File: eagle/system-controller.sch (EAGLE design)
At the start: 232 parts, among them CN1 22u, IC2 TS4100, J1 1, Q0 MOSFET-P-N-PAIR, Q1 MOSFET-P-N-PAIR, Q10 DNP/NTR4101P, Q12 DNP/NTR4101P, Q13 DON3035L, Q2 MOSFET-P-N-PAIR, Q3 MOSFET-P-N-PAIR, Q4 MOSFET-P-N-PAIR, Q5 MOSFET-P-N-PAIR, Q6 MOSFET-P-N-PAIR, Q7 MOSFET-P-N-PAIR, SW0 TPS25944LRVCRWQFN-20-3X4, SW1 TPS25944LRVCRWQFN-20-3X4, SW2 TPS25944LRVCRWQFN-20-3X4, SW3 TPS25944LRVCRWQFN-20-3X4, SW4 TPS25944LRVCRWQFN-20-3X4, SW5 TPS25944LRVCRWQFN-20-3X4, SW6 TPS25944LRVCRWQFN-20-3X4, SW7 TPS25944LRVCRWQFN-20-3X4, U1 MEGA128-A, X1 8 MHz CRYSTAL-ABRACON-ABM3-SMD

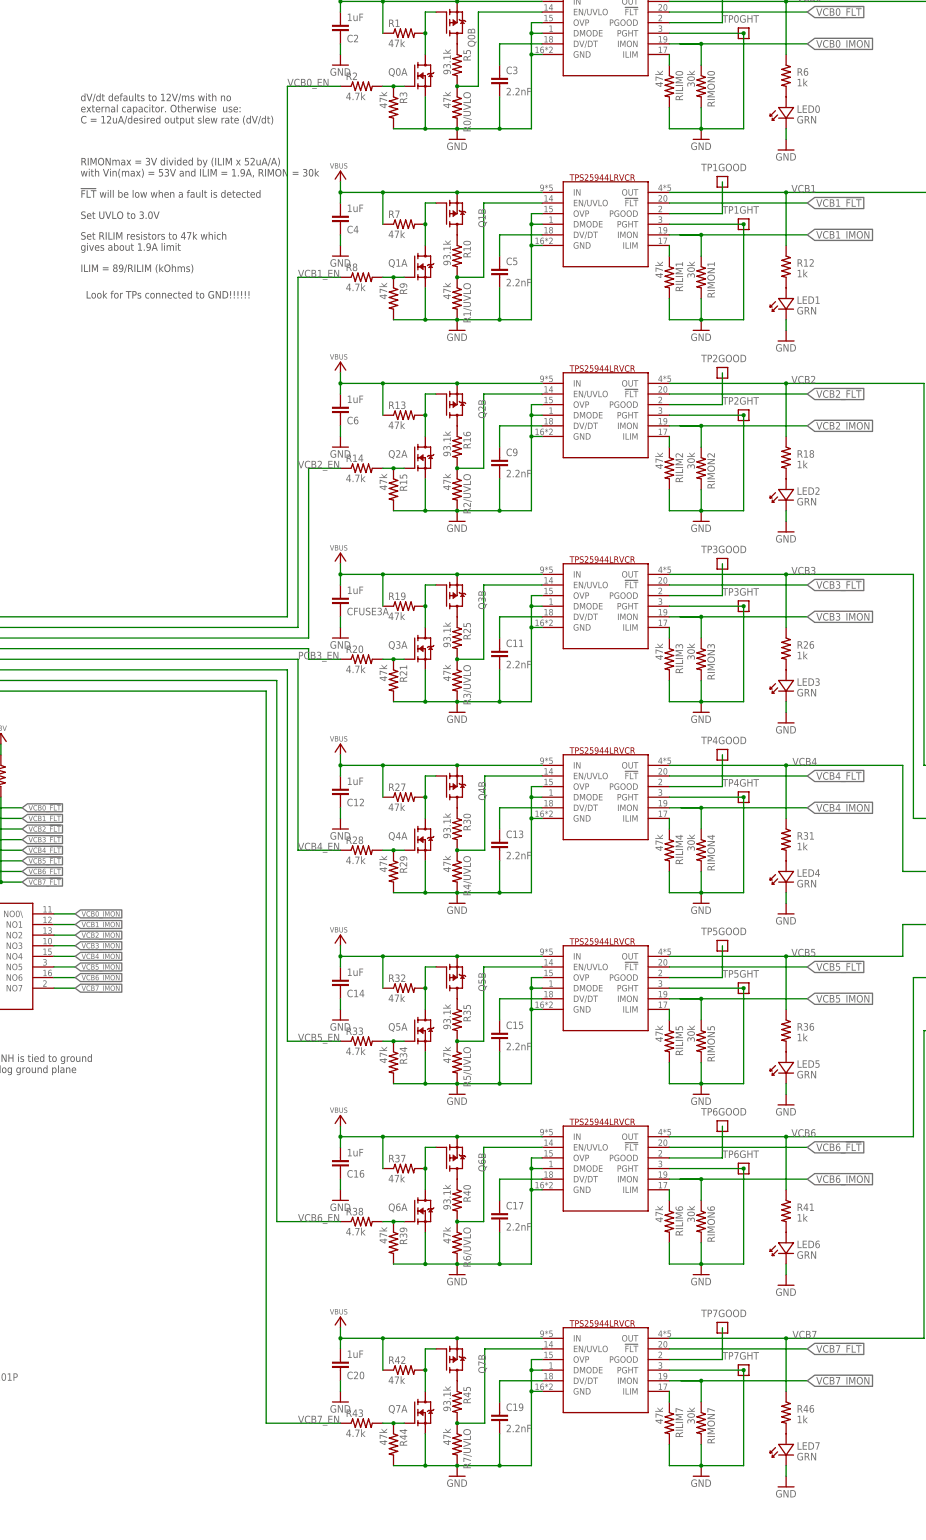
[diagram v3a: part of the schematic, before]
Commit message: Better layout for bypass caps ner AVR. Some cleanup on routing. Changed power domain indicators to DNP.
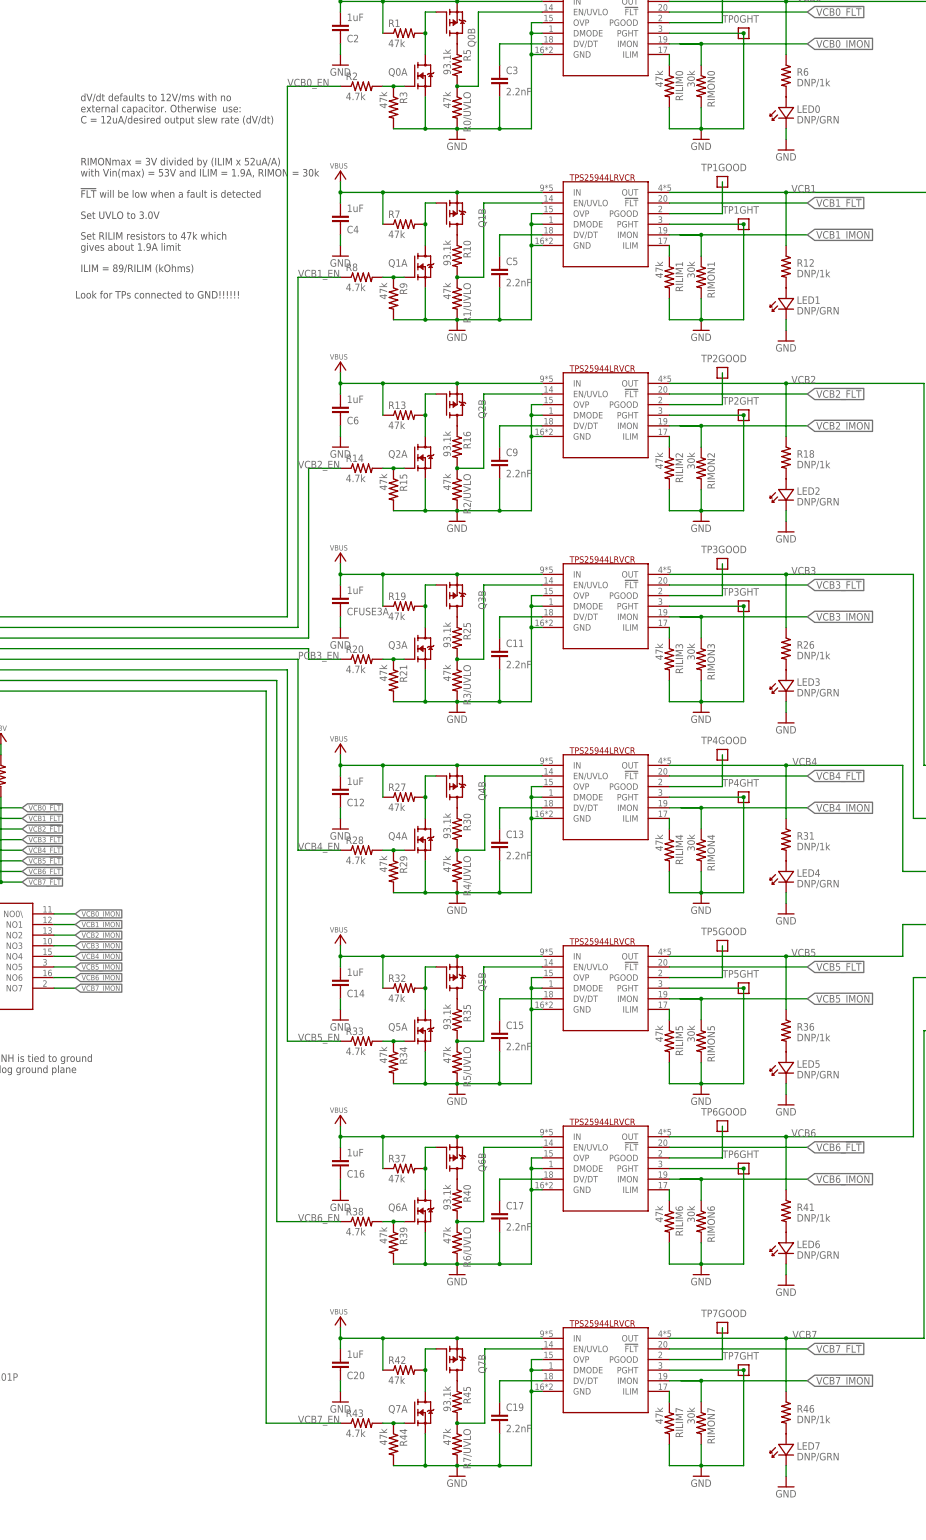
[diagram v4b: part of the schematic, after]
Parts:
- LED0, LED1, LED2, LED3, LED4, LED5, LED6, LED7: value GRN -> DNP/GRN
- R12, R18, R26, R31, R36, R41, R46, R6: value 1k -> DNP/1k
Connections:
- net N$36 renamed AREF
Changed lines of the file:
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@@
 <part name="3V-2" library="supply-3v" deviceset="3V" device=""/>
 <part name="3V-6" library="supply-3v" deviceset="3V" device=""/>
-<part name="LED0" library="psas_c3_team05" deviceset="LED" device="-0603" value="GRN">
+<part name="LED0" library="psas_c3_team05" deviceset="LED" device="-0603" value="DNP/GRN">
 <attribute name="DIST" value="digikey"/>
 <attribute name="DPN" value="732-4971-1-ND"/>
@@
 <attribute name="MPN" value="150060GS75000"/>
 </part>
-<part name="R6" library="rcl_custom" deviceset="R-US_" device="0603-B-NOSILK" value="1k">
+<part name="R6" library="rcl_custom" deviceset="R-US_" device="0603-B-NOSILK" value="DNP/1k">
 <attribute name="DIST" value="digikey"/>
 <attribute name="DPN" value="1276-3484-1-ND"/>
@@
 <attribute name="MPN" value="RC1608F472CS"/>
 </part>
-<part name="R12" library="rcl_custom" deviceset="R-US_" device="0603-B-NOSILK" value="1k">
+<part name="R12" library="rcl_custom" deviceset="R-US_" device="0603-B-NOSILK" value="DNP/1k">
 <attribute name="DIST" value="digikey"/>
 <attribute name="DPN" value="1276-3484-1-ND"/>
@@
 <attribute name="MPN" value="RC1608F102CS"/>
 </part>
-<part name="R18" library="rcl_custom" deviceset="R-US_" device="0603-B-NOSILK" value="1k">
+<part name="R18" library="rcl_custom" deviceset="R-US_" device="0603-B-NOSILK" value="DNP/1k">
 <attribute name="DIST" value="digikey"/>
 <attribute name="DPN" value="1276-3484-1-ND"/>
@@
 <attribute name="MPN" value="RC1608F102CS"/>
 </part>
-<part name="R26" library="rcl_custom" deviceset="R-US_" device="0603-B-NOSILK" value="1k">
+<part name="R26" library="rcl_custom" deviceset="R-US_" device="0603-B-NOSILK" value="DNP/1k">
 <attribute name="DIST" value="digikey"/>
 <attribute name="DPN" value="1276-3484-1-ND"/>
@@
 <attribute name="MPN" value="RC1608F102CS"/>
 </part>
-<part name="R31" library="rcl_custom" deviceset="R-US_" device="0603-B-NOSILK" value="1k">
+<part name="R31" library="rcl_custom" deviceset="R-US_" device="0603-B-NOSILK" value="DNP/1k">
 <attribute name="DIST" value="digikey"/>
 <attribute name="DPN" value="1276-3484-1-ND"/>
@@
 <attribute name="MPN" value="RC1608F102CS"/>
 </part>
-<part name="R36" library="rcl_custom" deviceset="R-US_" device="0603-B-NOSILK" value="1k">
+<part name="R36" library="rcl_custom" deviceset="R-US_" device="0603-B-NOSILK" value="DNP/1k">
 <attribute name="DIST" value="digikey"/>
 <attribute name="DPN" value="1276-3484-1-ND"/>
@@
 <attribute name="MPN" value="RC1608F102CS"/>
 </part>
-<part name="R41" library="rcl_custom" deviceset="R-US_" device="0603-B-NOSILK" value="1k">
+<part name="R41" library="rcl_custom" deviceset="R-US_" device="0603-B-NOSILK" value="DNP/1k">
 <attribute name="DIST" value="digikey"/>
 <attribute name="DPN" value="1276-3484-1-ND"/>
@@
 <attribute name="MPN" value="RC1608F102CS"/>
 </part>
-<part name="R46" library="rcl_custom" deviceset="R-US_" device="0603-B-NOSILK" value="1k">
+<part name="R46" library="rcl_custom" deviceset="R-US_" device="0603-B-NOSILK" value="DNP/1k">
 <attribute name="DIST" value="digikey"/>
 <attribute name="DPN" value="1276-3484-1-ND"/>
@@
 <attribute name="MPN" value="RC1608F102CS"/>
 </part>
-<part name="LED1" library="psas_c3_team05" deviceset="LED" device="-0603" value="GRN">
+<part name="LED1" library="psas_c3_team05" deviceset="LED" device="-0603" value="DNP/GRN">
 <attribute name="DIST" value="digikey"/>
 <attribute name="DPN" value="732-4971-1-ND"/>
@@
 <attribute name="MPN" value="150060GS75000"/>
 </part>
-<part name="LED2" library="psas_c3_team05" deviceset="LED" device="-0603" value="GRN">
+<part name="LED2" library="psas_c3_team05" deviceset="LED" device="-0603" value="DNP/GRN">
 <attribute name="DIST" value="digikey"/>
 <attribute name="DPN" value="732-4971-1-ND"/>
@@
 <attribute name="MPN" value="150060GS75000"/>
 </part>
-<part name="LED3" library="psas_c3_team05" deviceset="LED" device="-0603" value="GRN">
+<part name="LED3" library="psas_c3_team05" deviceset="LED" device="-0603" value="DNP/GRN">
 <attribute name="DIST" value="digikey"/>
 <attribute name="DPN" value="732-4971-1-ND"/>
@@
 <attribute name="MPN" value="150060GS75000"/>
 </part>
-<part name="LED4" library="psas_c3_team05" deviceset="LED" device="-0603" value="GRN">
+<part name="LED4" library="psas_c3_team05" deviceset="LED" device="-0603" value="DNP/GRN">
 <attribute name="DIST" value="digikey"/>
 <attribute name="DPN" value="732-4971-1-ND"/>
@@
 <attribute name="MPN" value="150060GS75000"/>
 </part>
-<part name="LED5" library="psas_c3_team05" deviceset="LED" device="-0603" value="GRN">
+<part name="LED5" library="psas_c3_team05" deviceset="LED" device="-0603" value="DNP/GRN">
 <attribute name="DIST" value="digikey"/>
 <attribute name="DPN" value="732-4971-1-ND"/>
@@
 <attribute name="MPN" value="150060GS75000"/>
 </part>
-<part name="LED6" library="psas_c3_team05" deviceset="LED" device="-0603" value="GRN">
+<part name="LED6" library="psas_c3_team05" deviceset="LED" device="-0603" value="DNP/GRN">
 <attribute name="DIST" value="digikey"/>
 <attribute name="DPN" value="732-4971-1-ND"/>
@@
 <attribute name="MPN" value="150060GS75000"/>
 </part>
-<part name="LED7" library="psas_c3_team05" deviceset="LED" device="-0603" value="GRN">
+<part name="LED7" library="psas_c3_team05" deviceset="LED" device="-0603" value="DNP/GRN">
 <attribute name="DIST" value="digikey"/>
 <attribute name="DPN" value="732-4971-1-ND"/>
@@
 When two pins are high the voltage at TP43 is 1.5V
 When all three pins are high the voltage at TP43 is 0.75V</text>
-<text x="309.88" y="345.44" size="1.778" layer="97">Look for TPs connected to GND!!!!!!</text>
+<text x="307.34" y="345.44" size="1.778" layer="97">Look for TPs connected to GND!!!!!!</text>
 </plain>
 <instances>
@@
 </segment>
 </net>
-<net name="N$36" class="0">
+<net name="AREF" class="0">
 <segment>
 <pinref part="U1" gate="G$1" pin="AREF"/>

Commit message: Added names to missing parts and updated the BOM and Parts Selection doc accordingly
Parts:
- removed U$1, U$2, U$3, U$4: ACPL-M61L, psas_c3_team05:ACPL-M61L
- removed U$8: AAT3215, psas_c3_team05:AAT3215
- added U2: LP5907MFX-3.0, system-controller:LP5907MFX-3.0
- added U3, U4, U5, U6: ACPL-M61L, system-controller:ACPL-M61L
- R17: DIST (none) -> digikey; DPN (none) -> A103093CT-ND; MFN (none) -> TE; MPN (none) -> 4-1676481-5
- renumbered CFUSE3A to C21, CLDO1 to C22, CLDO2 to C23, CLDO3 to C29, CN1 to C24, IC2 to U15, RLDO1 to R60, RN1 to R66, RN2 to R65, RN3 to R64, RN4 to R17, RNR to R62, SW0 to U7, SW1 to U8, SW2 to U9, SW3 to U10, SW4 to U11, SW5 to U12, SW6 to U13, SW7 to U14
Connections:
- net 3V: now also U2.VOUT, U4.VDD, U6.VDD; no longer U$2.VDD, U$4.VDD, U$8.VOUT
- net GND: now also U2.GND, U3.GND2, U4.GND2, U5.GND2, U6.GND2; no longer U$1.GND2, U$2.GND2, U$3.GND2, U$4.GND2, U$8.GND
- net N$16: now also U5.VOUT; no longer U$3.VOUT
- net N$18: now also U6.VOUT; no longer U$4.VOUT
- net N$22: now also U2.EN; no longer U$8.EN
- net N$23: now also U2.BYP; no longer U$8.BYP
- net N$24: now also U4.VOUT; no longer U$2.VOUT
- net N$4: now also U5.VIN; no longer U$3.VIN
- net N$5: now also U3.VOUT; no longer U$1.VOUT
- net N$54: now also U6.VIN; no longer U$4.VIN
- net N$58: now also U3.VIN; no longer U$1.VIN
- net N$8: now also U4.VIN; no longer U$2.VIN
- net TXD0: now also U5.GND1; no longer U$3.GND1
- net TXD1: now also U3.GND1; no longer U$1.GND1
- net UART_FC_TX: now also U4.GND1; no longer U$2.GND1
- net UART_FC_VCC: now also U3.VDD; no longer U$1.VDD
- net UART_LGR_TX: now also U6.GND1; no longer U$4.GND1
- net UART_LGR_VCC: now also U5.VDD; no longer U$3.VDD
- net V+: now also U2.VIN; no longer U$8.VIN

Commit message: More board cleanup!
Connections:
- net GND: now also CF3.19, CF3.29, CF3.39, CF3.9; no longer CF3.15, CF3.25, CF3.35, CF3.5
- net VCB1: now also CF3.5; no longer CF3.9
- net VCB3: now also CF3.15; no longer CF3.19
- net VCB5: now also CF3.25; no longer CF3.29
- net VCB7: now also CF3.35; no longer CF3.39

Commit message: Lots of board cleanup. Improved packages for ATMEGA, analog switch, and TPS. Re-did power polygons to tighten up the layout. Straightened wires because OCD, fixed DRCs.
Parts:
- removed C33, C34: 100nF, rcl_custom:C-EU0603-B-NOSILK
- removed LED0: DNP/GRN, psas_c3_team05:LED-0603
- removed Q0: MOSFET-P-N-PAIR, ic-transistor-mosfet-n-p:MOSFET-P-N-PAIR
- removed Q12: DNP/NTR4101P, Tova:NTR4101P
- removed Q13: DON3035L, adafruit:MOSFET-NREFLOW
- removed R0/UVLO, R1/UVLO, R2/UVLO, R3/UVLO, R4/UVLO, R5/UVLO, RA0, RA1, RA2, RA3, RA4, RA5, RA6, RA7, RILIM0: 47k, rcl_custom:R-US_0603-B-NOSILK
- removed RIMON0: 30k, rcl_custom:R-US_0603-B-NOSILK
- removed TP0GHT, TP1GHT, TP2GHT, TP3GHT, TP4GHT, TP5GHT, TP6GHT, TP7GHT: TEST-POINT, Tova:TEST-POINT
- added C10: 22u, rcl_custom:C-EU0603-B-NOSILK
- added C18: 100nF, rcl_custom:C-EU0603-B-NOSILK
- added LED12: DNP/AMB, psas_c3_team05:LED-0603
- added Q11, Q9: DNP/NTR4101P, Tova:NTR4101P
- added Q8: MOSFET-P-N-PAIR, ic-transistor-mosfet-n-p:MOSFET-P-N-PAIR
- added R52, R56, R63, R71, R75: DNP/1k, rcl_custom:R-US_0603-B-NOSILK
- added R55: 93.1k, rcl_custom:R-US_0603-B-NOSILK
- added R57, R67: 4.7k, rcl_custom:R-US_0603-B-NOSILK
- added R58, R68, RILIM8: 47k, rcl_custom:R-US_0603-B-NOSILK
- added R70, R72, R74: 390, rcl_custom:R-US_0603-B-NOSILK
- added R73: 1k, rcl_custom:R-US_0603-B-NOSILK
- added RIMON8: 30k, rcl_custom:R-US_0603-B-NOSILK
- C1: value CAP-ELNA-DS -> 1uF; device cap-elna-ds:CAP-ELNA-DS -> rcl_custom:C-EU0603-B-NOSILK; DPN 604-1020-1-ND -> 1276-1946-1-ND; MFN Elna America -> Samsung; MPN DSK-3R3H224U-HL -> CL10B105KP8NNNC
- C12: value 1uF -> 100nF; DPN 1276-1946-1-ND -> 399-1097-1-ND; MFN Samsung -> Kemet; MPN CL10B105KP8NNNC -> C0603C104J4RACTU
- C13, C19: value 2.2nF -> 100nF; DIST (none) -> digikey; DPN (none) -> 399-1097-1-ND; MFN (none) -> Kemet; MPN (none) -> C0603C104J4RACTU
- C15, C17: value 2.2nF -> 9pF; DIST (none) -> digikey; DPN (none) -> 399-11245-1-ND; MFN (none) -> Kemet; MPN (none) -> CBR02C909B5GAC
- C16, C2, C21: value 1uF -> 2.2nF; DIST digikey -> (none); DPN 1276-1946-1-ND -> (none); MFN Samsung -> (none); MPN CL10B105KP8NNNC -> (none)
- C23: value 10nF -> 1uF; DPN 399-1092-1-ND -> 1276-1946-1-ND; MFN Kemet -> Samsung; MPN C0603C103J5RACTU -> CL10B105KP8NNNC
- C24: value 22u -> 2.2nF; DIST digikey -> (none); DPN 399-1092-1-ND -> (none); MFN Kemet -> (none); MPN C0603C103J5RACTU -> (none)
- C26, C30: value 100nF -> 2.2nF; DIST digikey -> (none); DPN 399-1097-1-ND -> (none); MFN Kemet -> (none); MPN C0603C104J4RACTU -> (none)
- C29: value 2.2uF -> 1uF; DPN 1276-1183-1-ND -> 1276-1946-1-ND; MPN CL10A225KQ8NNNC -> CL10B105KP8NNNC
- C3: value 2.2nF -> CAP-ELNA-DS; device rcl_custom:C-EU0603-B-NOSILK -> cap-elna-ds:CAP-ELNA-DS; DIST (none) -> digikey; DPN (none) -> 604-1020-1-ND; MFN (none) -> Elna America; MPN (none) -> DSK-3R3H224U-HL
- C31, C32: DPN 399-1097-1-ND -> 490-6327-1-ND; MFN Kemet -> Murata; MPN C0603C104J4RACTU -> GRM155R71C104JA88D
- C4: value 1uF -> 10nF; DPN 1276-1946-1-ND -> 399-1092-1-ND; MFN Samsung -> Kemet; MPN CL10B105KP8NNNC -> C0603C103J5RACTU
- C5: value 2.2nF -> 2.2uF; DIST (none) -> digikey; DPN (none) -> 1276-1183-1-ND; MFN (none) -> Samsung; MPN (none) -> CL10A225KQ8NNNC
- C7: value 9pF -> 1uF; DPN 399-11245-1-ND -> 1276-1946-1-ND; MFN Kemet -> Samsung; MPN CBR02C909B5GAC -> CL10B105KP8NNNC
- C8: value 9pF -> 2.2nF; DIST digikey -> (none); DPN 399-11245-1-ND -> (none); MFN Kemet -> (none); MPN CBR02C909B5GAC -> (none)
- C9: value 2.2nF -> 1uF; DIST (none) -> digikey; DPN (none) -> 1276-1946-1-ND; MFN (none) -> Samsung; MPN (none) -> CL10B105KP8NNNC
- D1, D2: value SMD-DIODE-SCHOTTKY-40V-5A(DO-214AB)-SSC53L -> SSC53L
- LED10, LED8: value DNP/AMB -> DNP/GRN; DPN 475-2712-1-ND -> 732-4971-1-ND; MFN OSRAM Opto Semi, -> Wurth Electronics INC.; MPN LA L296-Q2R2-1-Z -> 150060GS75000
- LED7: value DNP/GRN -> DNP/AMB; DPN 732-4971-1-ND -> 475-2712-1-ND; MFN Wurth Electronics INC. -> OSRAM Opto Semi,; MPN 150060GS75000 -> LA L296-Q2R2-1-Z
- Q10: value DNP/NTR4101P -> MOSFET-P-N-PAIR; device Tova:NTR4101P -> ic-transistor-mosfet-n-p:MOSFET-P-N-PAIR; DPN NTR4101PT1HOSCT-ND -> DMG6601LVT-7DICT-ND; MFN ON Semiconductor -> Diodes Incorporated; MPN NTR4101PT1H -> DMG6601LVT-7
- Q3: value MOSFET-P-N-PAIR -> DON3035L; device ic-transistor-mosfet-n-p:MOSFET-P-N-PAIR -> adafruit:MOSFET-NREFLOW; DIST digikey -> (none); DPN DMG6601LVT-7DICT-ND -> (none); MFN Diodes Incorporated -> (none); MPN DMG6601LVT-7 -> (none)
- R10: value 93.1k -> DNP/1k; DPN 1276-4837-1-ND -> 1276-3484-1-ND; MPN RC1608F9312CS -> RC1608F102CS
- R11, R4, R49: value 390 -> 4.7k; DPN A103093CT-ND -> 1276-3502-1-ND; MFN TE -> Samsung; MPN 4-1676481-5 -> RC1608F472CS
- R12, R23, R24, R26, R31, R36, R46, R6: value DNP/1k -> 47k; DPN 1276-3484-1-ND -> 1276-4808-1-ND; MFN Samsung -> Samaung; MPN RC1608F102CS -> RC1608F473CS
- R14: value 4.7k -> 390; DPN 1276-3502-1-ND -> A103093CT-ND; MFN Samsung -> TE; MPN RC1608F472CS -> 4-1676481-5
- R15, R19: value 47k -> 390; DPN 1276-4808-1-ND -> A103093CT-ND; MFN Samaung -> TE; MPN RC1608F473CS -> 4-1676481-5
- R16, R25: value 93.1k -> 390; DPN 1276-4837-1-ND -> A103093CT-ND; MFN Samsung -> TE; MPN RC1608F9312CS -> 4-1676481-5
- R17, R50, R51, R53, R64: value 390 -> 47k; DPN A103093CT-ND -> 1276-4808-1-ND; MFN TE -> Samaung; MPN 4-1676481-5 -> RC1608F473CS
- R18: value DNP/1k -> 470k; DIST digikey -> (none); DPN 1276-3484-1-ND -> (none); MFN Samsung -> (none); MPN RC1608F102CS -> (none)
- R2, R20: value 4.7k -> 93.1k; DPN 1276-3502-1-ND -> 1276-4837-1-ND; MPN RC1608F472CS -> RC1608F9312CS
- R21, R3, R42: value 47k -> DNP/1k; DPN 1276-4808-1-ND -> 1276-3484-1-ND; MFN Samaung -> Samsung; MPN RC1608F473CS -> RC1608F102CS
- R22: value DNP/1k -> 4.7k; DPN 1276-3484-1-ND -> 1276-3502-1-ND; MPN RC1608F102CS -> RC1608F472CS
- R27, R9: value 47k -> 93.1k; DPN 1276-4808-1-ND -> 1276-4837-1-ND; MFN Samaung -> Samsung; MPN RC1608F473CS -> RC1608F9312CS
- R28: value 4.7k -> DNP/1k; DPN 1276-3502-1-ND -> 1276-3484-1-ND; MPN RC1608F472CS -> RC1608F102CS
- R29: value 47k -> 4.7k; DPN 1276-4808-1-ND -> 1276-3502-1-ND; MFN Samaung -> Samsung; MPN RC1608F473CS -> RC1608F472CS
- R30, R35, R40, R45, R5: value 93.1k -> 47k; DPN 1276-4837-1-ND -> 1276-4808-1-ND; MFN Samsung -> Samaung; MPN RC1608F9312CS -> RC1608F473CS
- R33, R38, R8: value 4.7k -> 47k; DPN 1276-3502-1-ND -> 1276-4808-1-ND; MFN Samsung -> Samaung; MPN RC1608F472CS -> RC1608F473CS
- R41: value DNP/1k -> 93.1k; DPN 1276-3484-1-ND -> 1276-4837-1-ND; MPN RC1608F102CS -> RC1608F9312CS
- R47, R65: value 390 -> 93.1k; DPN A103093CT-ND -> 1276-4837-1-ND; MFN TE -> Samsung; MPN 4-1676481-5 -> RC1608F9312CS
- R48, R66: value 390 -> DNP/1k; DPN A103093CT-ND -> 1276-3484-1-ND; MFN TE -> Samsung; MPN 4-1676481-5 -> RC1608F102CS
- R60: value 10k -> 390; DPN 1276-3485-1-ND -> A103093CT-ND; MFN Samsung -> TE; MPN RC1608F103CS -> 4-1676481-5
- R61: value DNP/1k -> 390; DPN 1276-3484-1-ND -> A103093CT-ND; MFN Samsung -> TE; MPN RC1608F102CS -> 4-1676481-5
- R62: value 470k -> 1k; DIST (none) -> digikey; DPN (none) -> A103093CT-ND; MFN (none) -> TE; MPN (none) -> 4-1676481-5
- R7: value 47k -> 10k; DPN 1276-4808-1-ND -> 1276-3485-1-ND; MFN Samaung -> Samsung; MPN RC1608F473CS -> RC1608F103CS
- U1: value MEGA128-A -> TPS25944LRVCRWQFN-20-3X4; device atmegas128:MEGA128-A -> system-controller:TPS25944LRVCRWQFN-20-3X4; MFN Atmel -> (none)
- U11, U12, U14: value TPS25944LRVCRWQFN-20-3X4 -> ACPL-M61L; device system-controller:TPS25944LRVCRWQFN-20-3X4 -> system-controller:ACPL-M61L
- U15: value TS4100 -> ACPL-M61L; device system-controller:TS4100 -> system-controller:ACPL-M61L
- U3, U4, U5, U6: value ACPL-M61L -> TPS25944LRVCRWQFN-20-3X4; device system-controller:ACPL-M61L -> system-controller:TPS25944LRVCRWQFN-20-3X4
- U7: value TPS25944LRVCRWQFN-20-3X4 -> ATMEGA128L-8A(U/N); device system-controller:TPS25944LRVCRWQFN-20-3X4 -> atmegas128:MEGA128-A; MFN (none) -> Atmel
- U8: value TPS25944LRVCRWQFN-20-3X4 -> TS4100; device system-controller:TPS25944LRVCRWQFN-20-3X4 -> system-controller:TS4100
- renumbered CF3 to CF2, R6/UVLO to R59, R7/UVLO to R69
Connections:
- net 3V: now also C12.2, C13.2, C18.2, C23.2, C5.1, Q11.S, Q9.S, R25.1, R32.1, R33.1, R34.1, R35.1, R36.1, R37.1, R38.1, R39.1, R52.1, R61.2, R70.2, R71.1, R74.2, U12.VDD, U7.AVCC, U7.VCC, U7.VCC@1, U8.VDD; no longer C25.2, C26.2, C29.1, C30.2, C34.2, Q10.S, Q12.S, R11.2, R22.1, R4.1, R48.2, R49.2, R61.1, RA0.1, RA1.1, RA2.1, RA3.1, RA4.1, RA5.1, RA6.1, RA7.1, U1.AVCC, U1.VCC, U1.VCC@1, U4.VDD, U6.VDD
- net AREF: now also C19.2, U7.AREF; no longer C27.2, U1.AREF
- net GND: now also C1.1, C10.2, C13.1, C15.1, C16.2, C17.1, C18.1, C19.1, C2.2, C21.2, C23.1, C26.2, C29.1, C3.-, C30.2, C4.2, C8.2, C9.1, LED10.K, LED12.K, LED8.K, Q10A.S, Q3.S, Q8A.S, R12.2, R13.2, R18.2, R19.2, R23.2, R24.2, R30.2, R31.2, R45.2, R5.2, R50.2, R51.2, R58.2, R6.2, R68.2, RILIM8.2, RIMON8.2, U1.DMODE, U1.OVP, U1.PGHT, U11.GND2, U12.GND2, U14.GND2, U15.GND2, U3.DMODE, U3.GND, U3.OVP, U3.PGHT, U4.DMODE, U4.GND, U4.OVP, U4.PGHT, U5.DMODE, U5.GND, U5.OVP, U5.PGHT, U6.DMODE, U6.GND, U6.OVP, U6.PGHT, U7.GND@1, U7.GND@2, U8.INH; no longer C1.-, C13.2, C15.2, C16.1, C17.2, C19.2, C2.1, C21.1, C23.2, C26.1, C29.2, C3.2, C30.1, C33.1, C34.1, C4.1, C8.1, C9.2, LED0.K, LED11.K, LED7.K, Q0A.S, Q13.S, Q3A.S, R0/UVLO.2, R1/UVLO.2, R15.2, R17.2, R2/UVLO.2, R21.2, R29.2, R3.2, R3/UVLO.2, R34.2, R39.2, R4/UVLO.2, R5/UVLO.2, R62.2, R9.2, RILIM0.2, RIMON0.2, TP0GHT.1, TP1GHT.1, TP2GHT.1, TP3GHT.1, TP4GHT.1, TP5GHT.1, TP6GHT.1, TP7GHT.1, U1.GND@1, U1.GND@2, U11.DMODE, U11.GND, U11.OVP, U11.PGHT, U12.DMODE, U12.GND, U12.OVP, U12.PGHT, U14.DMODE, U14.GND, U14.OVP, U14.PGHT, U15.GND, U15.INH, U3.GND2, U4.GND2, U5.GND2, U6.GND2, U7.DMODE, U7.OVP, U7.PGHT, U8.DMODE, U8.OVP, U8.PGHT
- net I2C-SCL: now also U7.(SCL/INT0)PD0; no longer U1.(SCL/INT0)PD0
- net I2C-SDA: now also U7.(SDA/INT1)PD1; no longer U1.(SDA/INT1)PD1
- net INOF: now also C2.1, U1.DV/DT; no longer C3.1, U7.DV/DT
- net N$1: now also C17.2, U7.XTAL1; no longer C8.2, U1.XTAL1
- net N$10: now also R20.2, R24.1, U4.EN/UVLO; no longer R16.2, R2/UVLO.1, U9.EN/UVLO
- net N$100: now also RILIM7.1, U10.ILIM; no longer RILIM6.1, U13.ILIM
- net N$101: now also U10.PGOOD; no longer U13.PGOOD
- net N$102: now also C26.1, U10.DV/DT; no longer C17.1, U13.DV/DT
- net N$103: now also Q8A.G, R57.2, R58.1; no longer Q6A.G, R38.2, R39.1
- net N$104: now also U7.(T2)PD7; no longer U1.(T2)PD7
- net N$105: now also Q8A.D, Q8B.G, R53.2; no longer Q6A.D, Q6B.G, R37.2
- net N$106: now also C10.1, Q3.G, R18.1; no longer C24.1, Q13.G, R62.1
- net N$107: now also U7.PF0(ADC0), U8.COMM; no longer U1.PF0(ADC0), U15.COMM
- net N$108: now also Q7B.D, R47.1; no longer Q5B.D, R35.1
- net N$109: now also R14.1, R15.1, R16.1, R19.1; no longer R17.1, R64.1, R65.1, R66.1
- net N$11: now also U7.PF4(ADC4/TCK); no longer U1.PF4(ADC4/TCK)
- net N$110: now also Q10B.D, R65.1; no longer Q7B.D, R45.1
- net N$111: now also Q8B.D, R55.1; no longer Q6B.D, R40.1
- net N$12: now also U7.PF6(ADC6/TDO); no longer U1.PF6(ADC6/TDO)
- net N$13: now also U7.PF5(ADC5/TMS); no longer U1.PF5(ADC5/TMS)
- net N$14: now also U7.PF7(ADC7/TDI); no longer U1.PF7(ADC7/TDI)
- net N$15: now also R25.2, U7.RESET; no longer R4.2, U1.RESET
- net N$16: now also R73.2, U14.VOUT; no longer R51.2, U5.VOUT
- net N$17: now also C15.2, U7.XTAL2; no longer C7.2, U1.XTAL2
- net N$18: now also R72.1, U15.VOUT; no longer R53.1, U6.VOUT
- net N$19: now also RILIM3.1, U4.ILIM; no longer RILIM2.1, U9.ILIM
- net N$2: now also Q2B.D, R9.1; no longer Q1B.D, R10.1
- net N$21: now also RILIM1.1, U1.ILIM; no longer RILIM0.1, U7.ILIM
- net N$22: now also R7.2; no longer R60.2
- net N$23: now also C4.1; no longer C23.1
- net N$24: now also R60.2, U12.VOUT; no longer R50.2, U4.VOUT
- net N$25: now also U1.PGOOD; no longer U7.PGOOD
- net N$26: now also LED1.A, R3.2; no longer LED0.A, R6.2
- net N$27: now also U7.PG3(TOSC2); no longer U1.PG3(TOSC2)
- net N$28: now also U7.PG4(TOSC1); no longer U1.PG4(TOSC1)
- net N$29: now also R13.1, R9.2, U3.EN/UVLO; no longer R1/UVLO.1, R10.2, U8.EN/UVLO
- net N$30: now also RILIM2.1, U3.ILIM; no longer RILIM1.1, U8.ILIM
- net N$32: now also U3.PGOOD; no longer U8.PGOOD
- net N$33: now also U7.PEN; no longer U1.PEN
- net N$34: now also U7.PF3(ADC3); no longer U1.PF3(ADC3)
- net N$35: now also U7.PF2(ADC2); no longer U1.PF2(ADC2)
- net N$37: now also U7.PF1(ADC1); no longer U1.PF1(ADC1)
- net N$38: now also C8.1, U3.DV/DT; no longer C5.1, U8.DV/DT
- net N$39: now also U7.(XCK0/AIN0)PE2; no longer U1.(XCK0/AIN0)PE2
- net N$4: now also R70.1, U14.VIN; no longer R54.1, U5.VIN
- net N$40: now also U7.(OC3A/AIN1)PE3; no longer U1.(OC3A/AIN1)PE3
- net N$41: now also U7.(OC3B/INT4)PE4; no longer U1.(OC3B/INT4)PE4
- net N$42: now also U7.(OC3C/INT5)PE5; no longer U1.(OC3C/INT5)PE5
- net N$43: now also U7.(T3/INT6)PE6; no longer U1.(T3/INT6)PE6
- net N$44: now also U7.(IC3/INT7)PE7; no longer U1.(IC3/INT7)PE7
- net N$45: now also LED2.A, R10.2; no longer LED1.A, R12.2
- net N$46: now also U7.(IC1)PD4, U8.ADDC; no longer U1.(IC1)PD4, U15.ADDC
- net N$47: now also U7.(XCK1)PD5, U8.ADDB; no longer U1.(XCK1)PD5, U15.ADDB
- net N$48: now also U7.(T1)PD6, U8.ADDA; no longer U1.(T1)PD6, U15.ADDA
- net N$49: now also Q2A.G, R11.2, R12.1; no longer Q1A.G, R8.2, R9.1
- net N$5: now also R62.2, U11.VOUT; no longer R47.2, U3.VOUT
- net N$50: now also Q1A.G, R4.2, R5.1; no longer Q0A.G, R2.2, R3.1
- net N$51: now also Q2A.D, Q2B.G, R8.2; no longer Q1A.D, Q1B.G, R7.2
- net N$52: now also LED3.A, R21.2; no longer LED2.A, R18.2
- net N$53: now also LED12.A, R75.2; no longer LED11.A, R23.2
- net N$54: now also R74.1, U15.VIN; no longer R11.1, U6.VIN
- net N$55: now also Q11.D, R75.1; no longer Q12.D, R23.1
- net N$56: now also LED7.A, R52.2; no longer LED10.A, R22.2
- net N$57: now also LED11.A, R71.2; no longer LED8.A, R61.2
- net N$58: now also R54.1, U11.VIN; no longer R49.1, U3.VIN
- net N$59: now also U4.PGOOD; no longer U9.PGOOD
- net N$60: now also R63.2; no longer R24.2
- net N$61: now also Q9.D, R63.1; no longer Q10.D, R24.1
- net N$62: now also C11.1, U4.DV/DT; no longer C9.1, U9.DV/DT
- net N$63: now also Q4A.G, R22.2, R23.1; no longer Q2A.G, R14.2, R15.1
- net N$64: now also Q4B.D, R20.1; no longer Q2B.D, R16.1
- net N$65: now also Q4A.D, Q4B.G, R17.2; no longer Q2A.D, Q2B.G, R13.2
- net N$66: now also LED4.A, R28.2; no longer LED3.A, R26.2
- net N$67: now also R65.2, U13.EN/UVLO; no longer R45.2, U14.EN/UVLO
- net N$68: now also RILIM8.1, U13.ILIM; no longer RILIM7.1, U14.ILIM
- net N$69: now also U13.PGOOD; no longer U14.PGOOD
- net N$70: now also C30.1, U13.DV/DT; no longer C19.1, U14.DV/DT
- net N$71: now also Q10A.G, R67.2, R68.1; no longer Q7A.G, R43.2, R44.1
- net N$72: now also Q1A.D, Q1B.G; no longer Q0A.D, Q0B.G
- net N$73: now also Q10A.D, Q10B.G, R64.2; no longer Q7A.D, Q7B.G, R42.2
- net N$74: now also LED5.A, R42.2; no longer LED4.A, R31.2
- net N$75: now also R47.2, R51.1, U9.EN/UVLO; no longer R35.2, R5/UVLO.1, U12.EN/UVLO
- net N$76: now also RILIM6.1, U9.ILIM; no longer RILIM5.1, U12.ILIM
- net N$77: now also U9.PGOOD; no longer U12.PGOOD
- net N$78: now also C24.1, U9.DV/DT; no longer C15.1, U12.DV/DT
- net N$79: now also Q7A.G, R49.2, R50.1; no longer Q5A.G, R33.2, R34.1
- net N$8: now also R61.1, U12.VIN; no longer R48.1, U4.VIN
- net N$80: now also Q1B.D, R2.1; no longer Q0B.D, R5.1
- net N$81: now also Q7A.D, Q7B.G, R46.2; no longer Q5A.D, Q5B.G, R32.2
- net N$82: now also LED6.A, R48.2; no longer LED5.A, R36.2
- net N$83: now also R41.2, R45.1, U6.EN/UVLO; no longer R30.2, R4/UVLO.1, U11.EN/UVLO
- net N$84: now also RILIM5.1, U6.ILIM; no longer RILIM4.1, U11.ILIM
- net N$85: now also U6.PGOOD; no longer U11.PGOOD
- net N$86: now also C21.1, U6.DV/DT; no longer C13.1, U11.DV/DT
- net N$87: now also Q6A.G, R43.2, R44.1; no longer Q4A.G, R28.2, R29.1
- net N$88: now also Q5B.D, R27.1; no longer Q3B.D, R25.1
- net N$89: now also Q6A.D, Q6B.G, R40.2; no longer Q4A.D, Q4B.G, R27.2
- net N$9: now also R2.2, R6.1, U1.EN/UVLO; no longer R0/UVLO.1, R5.2, U7.EN/UVLO
- net N$90: now also LED8.A, R56.2; no longer LED6.A, R41.2
- net N$91: now also R27.2, R31.1, U5.EN/UVLO; no longer R25.2, R3/UVLO.1, U10.EN/UVLO
- net N$92: now also RILIM4.1, U5.ILIM; no longer RILIM3.1, U10.ILIM
- net N$93: now also U5.PGOOD; no longer U10.PGOOD
- net N$94: now also C16.1, U5.DV/DT; no longer C11.1, U10.DV/DT
- net N$95: now also Q5A.G, R29.2, R30.1; no longer Q3A.G, R20.2, R21.1
- net N$96: now also Q6B.D, R41.1; no longer Q4B.D, R30.1
- net N$97: now also Q5A.D, Q5B.G, R26.2; no longer Q3A.D, Q3B.G, R19.2
- net N$98: now also LED10.A, R66.2; no longer LED7.A, R46.2
- net N$99: now also R55.2, U10.EN/UVLO; no longer R40.2, U13.EN/UVLO
- net NUCLEAROPTION0: now also R16.2, U7.PG0(WR); no longer R64.2, U1.PG0(WR)
- net NUCLEAROPTION1: now also R15.2, U7.PG1(RD); no longer R65.2, U1.PG1(RD)
- net NUCLEAROPTION2: now also R14.2, U7.PG2(ALE); no longer R66.2, U1.PG2(ALE)
- net NUCLEAROPTION_OUT: now also Q3.D; no longer Q13.D
- net PB0: now also U7.(SS)PB0; no longer U1.(SS)PB0
- net PB1: now also U7.(SCK)PB1; no longer U1.(SCK)PB1
- net PB2: now also U7.(MOSI)PB2; no longer U1.(MOSI)PB2
- net PB3: now also U7.(MISO)PB3; no longer U1.(MISO)PB3
- net PB4: now also U7.(OC0)PB4; no longer U1.(OC0)PB4
- net PB5: now also U7.(OC1A)PB5; no longer U1.(OC1A)PB5
- net PB6: now also U7.(OC1B)PB6; no longer U1.(OC1B)PB6
- net PB7: now also U7.(OC2/OC1C)PB7; no longer U1.(OC2/OC1C)PB7
- net PCB3_EN: now also R29.1, U7.(AD4)PA4; no longer R20.1, U1.(AD4)PA4
- net RXD0: now also Q11.G, R72.2, U7.(RXD/PDI)PE0; no longer Q12.G, R53.2, U1.(RXD/PDI)PE0
- net RXD1: now also Q9.G, R60.1, U7.(RXD1/INT2)PD2; no longer Q10.G, R50.1, U1.(RXD1/INT2)PD2
- net TXD0: now also LED11.K, U14.GND1, U7.(TXD/PDO)PE1; no longer LED8.K, U1.(TXD/PDO)PE1, U5.GND1
- net TXD1: now also LED7.K, U11.GND1, U7.(TXD1/INT3)PD3; no longer LED10.K, U1.(TXD1/INT3)PD3, U3.GND1
- net UART_FC_RX: now also R62.1; no longer R47.1
- net UART_FC_TX: now also U12.GND1; no longer U4.GND1
- net UART_FC_VCC: now also C27.2, U11.VDD; no longer C31.2, U3.VDD
- net UART_LGR_RX: now also R73.1; no longer R51.1
- net UART_LGR_TX: now also U15.GND1; no longer U6.GND1
- net UART_LGR_VCC: now also C31.2, U14.VDD; no longer C33.2, U5.VDD
- net V+: now also C3.+, C6.2, R7.1; no longer C1.+, C22.2, R60.1
- net VBUS: now also C1.2, C22.2, C25.2, C29.2, C7.2, C9.2, Q10B.S, Q8B.S, R17.1, R26.1, R40.1, R46.1, R53.1, R64.1, R8.1, U1.IN, U3.IN, U4.IN, U5.IN, U6.IN; no longer C12.2, C16.2, C2.2, C21.2, C4.2, C6.2, Q0B.S, Q3B.S, R13.1, R19.1, R27.1, R32.1, R37.1, R42.1, R7.1, U11.IN, U12.IN, U14.IN, U7.IN, U8.IN
- net VCB0: now also R3.1, U1.OUT; no longer R6.1, U7.OUT
- net VCB0_!FLT: now also R32.2, U1.!FLT, U7.(A15)PC7; no longer RA0.2, U1.(A15)PC7, U7.!FLT
- net VCB0_EN: now also R4.1, U7.(AD7)PA7; no longer R2.1, U1.(AD7)PA7
- net VCB0_IMON: now also RIMON1.1, U1.IMON, U8.NO0\; no longer RIMON0.1, U15.NO0\, U7.IMON
- net VCB1: now also R10.1, U3.OUT; no longer R12.1, U8.OUT
- net VCB1_!FLT: now also R33.2, U3.!FLT, U7.(A14)PC6; no longer RA1.2, U1.(A14)PC6, U8.!FLT
- net VCB1_EN: now also R11.1, U7.(AD6)PA6; no longer R8.1, U1.(AD6)PA6
- net VCB1_IMON: now also RIMON2.1, U3.IMON, U8.NO1; no longer RIMON1.1, U15.NO1, U8.IMON
- net VCB2: now also R21.1, U4.OUT; no longer R18.1, U9.OUT
- net VCB2_!FLT: now also R34.2, U4.!FLT, U7.(A13)PC5; no longer RA2.2, U1.(A13)PC5, U9.!FLT
- net VCB2_EN: now also R22.1, U7.(AD5)PA5; no longer R14.1, U1.(AD5)PA5
- net VCB2_IMON: now also RIMON3.1, U4.IMON, U8.NO2; no longer RIMON2.1, U15.NO2, U9.IMON
- net VCB3: now also R28.1, U5.OUT; no longer R26.1, U10.OUT
- net VCB3_!FLT: now also R35.2, U5.!FLT, U7.(A12)PC4; no longer RA3.2, U1.(A12)PC4, U10.!FLT
- net VCB3_IMON: now also RIMON4.1, U5.IMON, U8.NO3; no longer RIMON3.1, U10.IMON, U15.NO3
- net VCB4: now also R42.1, U6.OUT; no longer R31.1, U11.OUT
- net VCB4_!FLT: now also R36.2, U6.!FLT, U7.(A11)PC3; no longer RA4.2, U1.(A11)PC3, U11.!FLT
- net VCB4_EN: now also R43.1, U7.(AD3)PA3; no longer R28.1, U1.(AD3)PA3
- net VCB4_IMON: now also RIMON5.1, U6.IMON, U8.NO4; no longer RIMON4.1, U11.IMON, U15.NO4
- net VCB5: now also R48.1, U9.OUT; no longer R36.1, U12.OUT
- net VCB5_!FLT: now also R37.2, U7.(A10)PC2, U9.!FLT; no longer RA5.2, U1.(A10)PC2, U12.!FLT
- net VCB5_EN: now also R49.1, U7.(AD2)PA2; no longer R33.1, U1.(AD2)PA2
- net VCB5_IMON: now also RIMON6.1, U8.NO5, U9.IMON; no longer RIMON5.1, U12.IMON, U15.NO5
- net VCB6: now also R56.1, U10.OUT; no longer R41.1, U13.OUT
- net VCB6_!FLT: now also R38.2, U10.!FLT, U7.(A9)PC1; no longer RA6.2, U1.(A9)PC1, U13.!FLT
- net VCB6_EN: now also R57.1, U7.(AD1)PA1; no longer R38.1, U1.(AD1)PA1
- net VCB6_IMON: now also RIMON7.1, U10.IMON, U8.NO6; no longer RIMON6.1, U13.IMON, U15.NO6
- net VCB7: now also R66.1, U13.OUT; no longer R46.1, U14.OUT
- net VCB7_!FLT: now also R39.2, U13.!FLT, U7.(A8)PC0; no longer RA7.2, U1.(A8)PC0, U14.!FLT
- net VCB7_EN: now also R67.1, U7.(AD0)PA0; no longer R43.1, U1.(AD0)PA0
- net VCB7_IMON: now also RIMON8.1, U13.IMON, U8.NO7; no longer RIMON7.1, U14.IMON, U15.NO7
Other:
- note added: "UART0 RX (from LGR)"
- note added: "UART0 TX (to LGR)"
- note added: "UART1 RX (from FC)"
- note added: "UART1 TX (to FC)"
- note removed: "P-Channel MOSFET"
- note removed: "UART0 RX"
- note removed: "UART0 TX"
- note removed: "UART1 RX"
- note removed: "UART1 TX"
- moved on the sheet: C11, C12, C13, C14, C15, C16, C17, C19, C2, C20, C21, C22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
